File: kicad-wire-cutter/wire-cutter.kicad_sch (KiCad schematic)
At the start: 17 parts, among them J1 Conn_01x01_Socket, J3 Conn_01x01_Socket, U4 ESP32-DEVKIT-V1

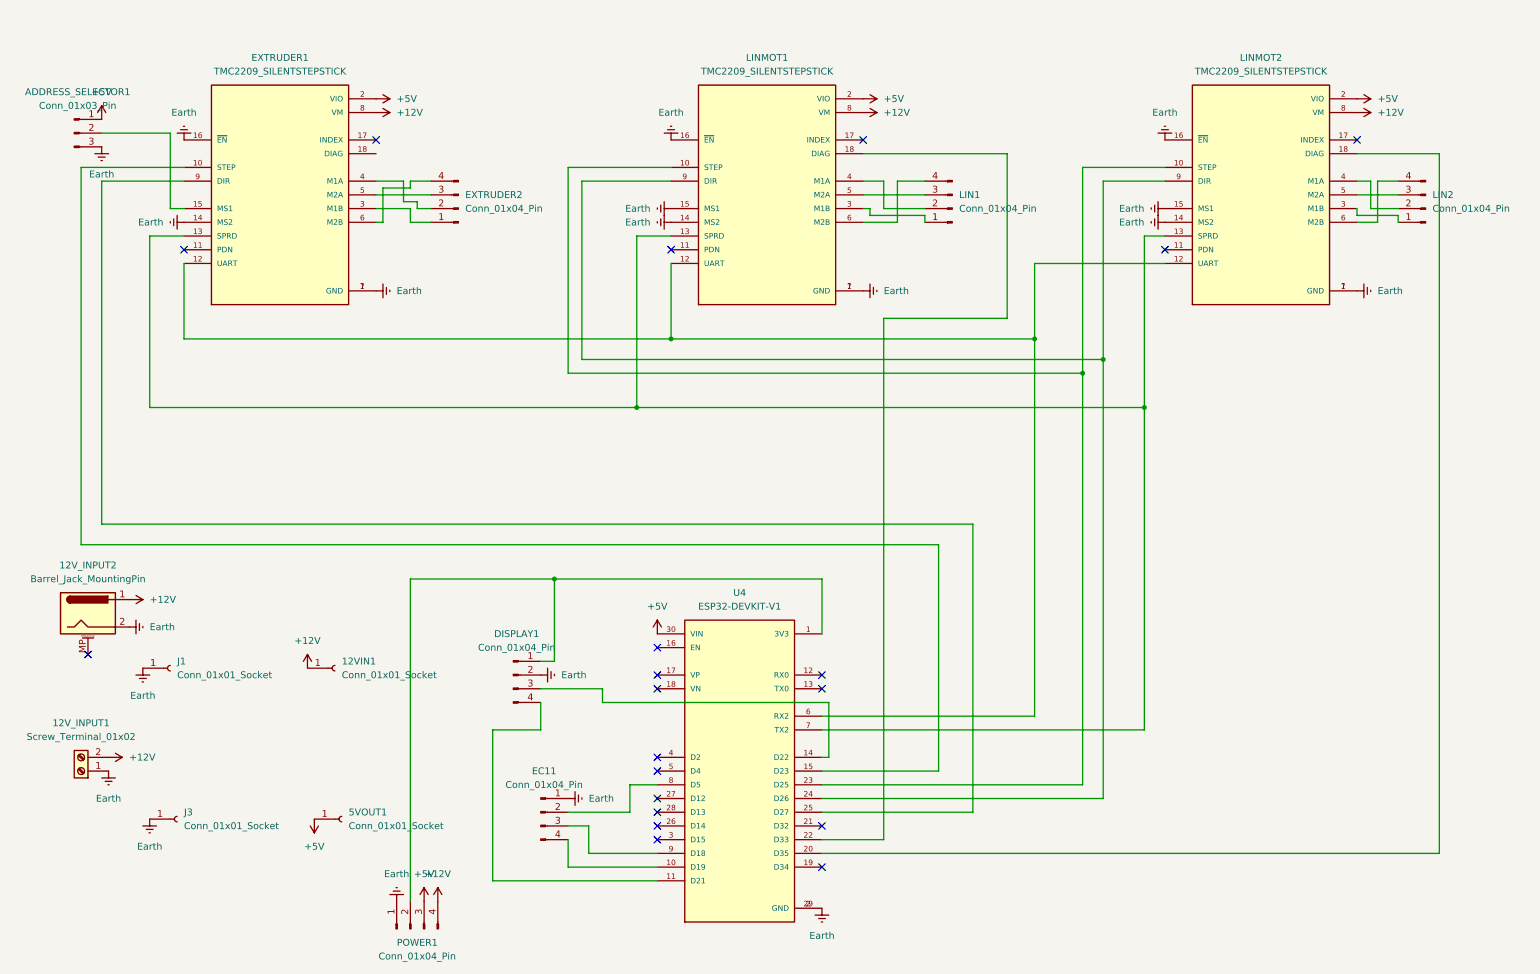
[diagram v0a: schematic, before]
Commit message: Finished full cut process
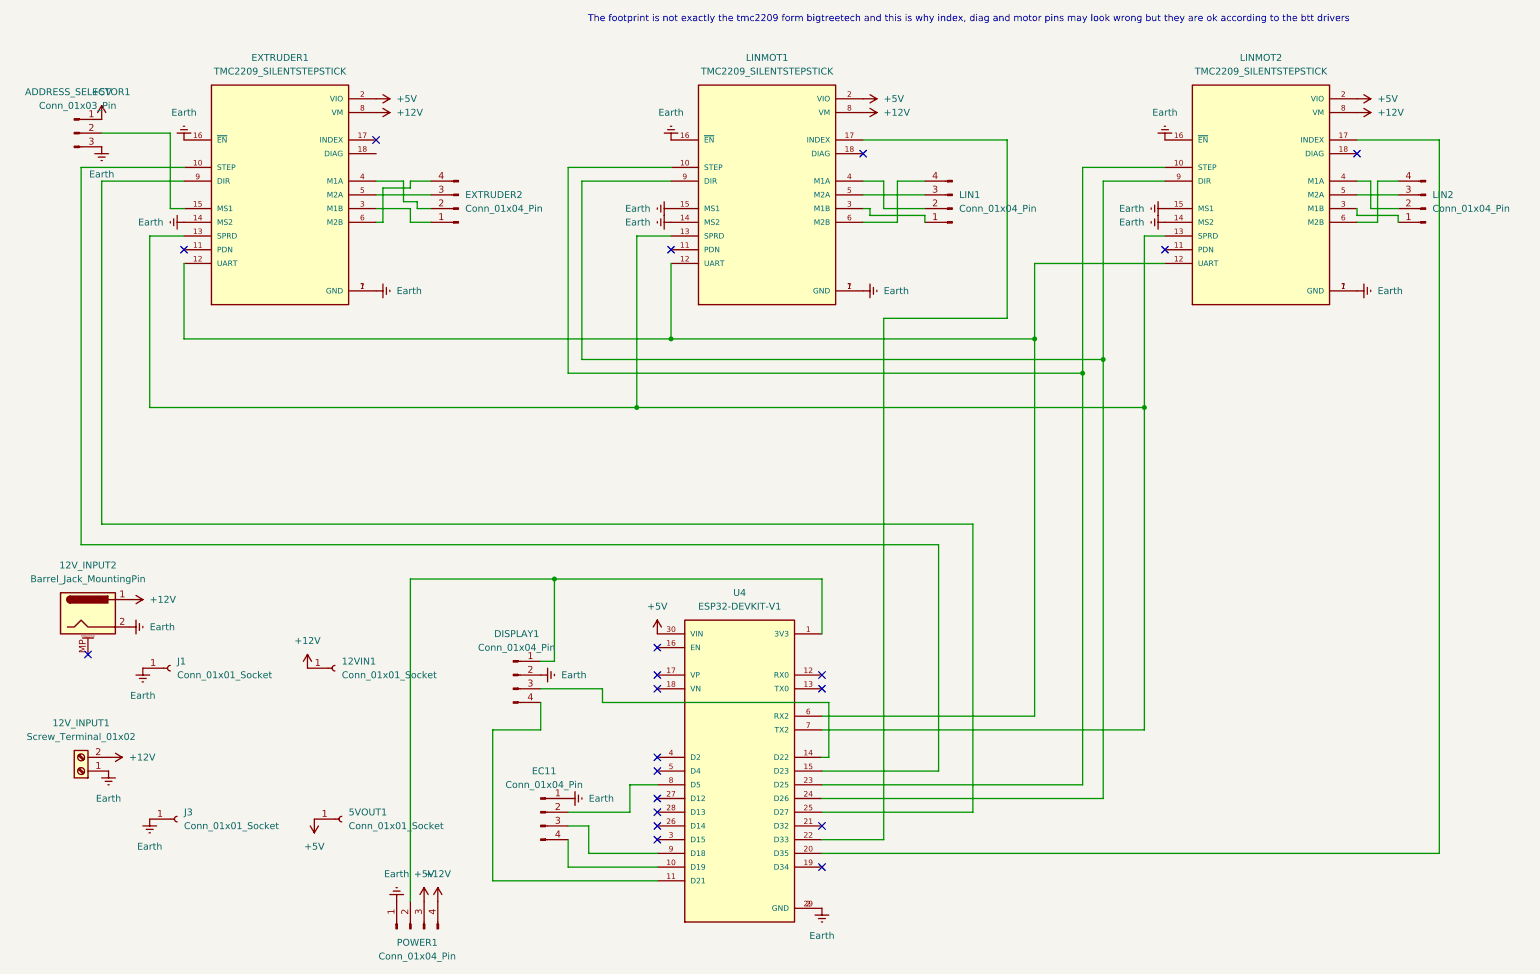
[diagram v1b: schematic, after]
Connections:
- net at U4.20 (D35): now also LINMOT2.17 (INDEX); no longer LINMOT2.18 (DIAG)
- net at U4.22 (D33): now also LINMOT1.17 (INDEX); no longer LINMOT1.18 (DIAG)
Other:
- note added: "The footprint is not exactly the tmc2209 form bigtreetech and this is why index, diag and motor pins may look wrong but they are ok according to the btt drivers"
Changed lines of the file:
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@@
-	)
-	(no_connect
-		(at 163.83 41.91)
 	)
 	(no_connect
@@
 	)
 	(no_connect
-		(at 255.27 41.91)
-	)
-	(no_connect
 		(at 125.73 135.89)
 	)
@@
 	)
 	(no_connect
+		(at 255.27 44.45)
+	)
+	(no_connect
 		(at 125.73 140.97)
 	)
@@
 	)
 	(no_connect
+		(at 163.83 44.45)
+	)
+	(no_connect
 		(at 156.21 168.91)
 	)
@@
 	(wire
 		(pts
-			(xy 270.51 44.45) (xy 270.51 173.99)
-		)
-		(stroke
-			(width 0)
-			(type default)
-		)
-	)
-	(wire
-		(pts
 			(xy 208.28 49.53) (xy 219.71 49.53)
 		)
@@
 	(wire
 		(pts
+			(xy 163.83 41.91) (xy 190.5 41.91)
+		)
+		(stroke
+			(width 0)
+			(type default)
+		)
+	)
+	(wire
+		(pts
 			(xy 156.21 151.13) (xy 215.9 151.13)
 		)
@@
 	(wire
 		(pts
+			(xy 270.51 41.91) (xy 270.51 173.99)
+		)
+		(stroke
+			(width 0)
+			(type default)
+		)
+	)
+	(wire
+		(pts
 			(xy 125.73 161.29) (xy 120.65 161.29)
 		)
@@
 	(wire
 		(pts
+			(xy 255.27 41.91) (xy 270.51 41.91)
+		)
+		(stroke
+			(width 0)
+			(type default)
+		)
+	)
+	(wire
+		(pts
 			(xy 31.75 59.69) (xy 31.75 91.44)
 		)
@@
 	(wire
 		(pts
-			(xy 190.5 74.93) (xy 190.5 44.45)
+			(xy 190.5 41.91) (xy 190.5 74.93)
 		)
 		(stroke
@@
 	(wire
 		(pts
-			(xy 255.27 44.45) (xy 270.51 44.45)
-		)
-		(stroke
-			(width 0)
-			(type default)
-		)
-	)
-	(wire
-		(pts
 			(xy 156.21 133.35) (xy 156.21 123.19)
 		)
@@
 		)
 	)
-	(wire
-		(pts
-			(xy 190.5 44.45) (xy 163.83 44.45)
-		)
-		(stroke
-			(width 0)
-			(type default)
-		)
-	)
+	(text "The footprint is not exactly the tmc2209 form bigtreetech and this is why index, diag and motor pins may look wrong but they are ok according to the btt drivers"
+		(exclude_from_sim no)
+		(at 183.388 19.558 0)
+		(effects
+			(font
+				(size 1.27 1.27)
+			)
+		)
+	)
